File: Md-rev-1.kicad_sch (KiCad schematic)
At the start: 24 parts, among them CN1 JSTPH, J1 USB_C_Receptacle_USB2.0, J2 AudioJack4_SwitchTR1, U1 MCP73831-2-OT, U2 MAX9814

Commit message: Updated the schematic & PCB
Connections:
- net GND: no longer S1.2
- net VBAT: now also S1.2; no longer C2.1, S1.3, U1.3 (V_{BAT})
- net at S1.1: now also C2.1, U1.3 (V_{BAT})
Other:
- moved on the sheet: CN1, S1
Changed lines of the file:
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@@
   (junction (at 180.34 118.11) (diameter 0) (color 0 0 0 0)
   )
-  (junction (at 144.78 152.4) (diameter 0) (color 0 0 0 0)
+  (junction (at 158.75 121.92) (diameter 0) (color 0 0 0 0)
   )
   (junction (at 123.19 124.46) (diameter 0) (color 0 0 0 0)
@@
   (junction (at 34.29 148.59) (diameter 0) (color 0 0 0 0)
   )
-  (junction (at 147.32 124.46) (diameter 0) (color 0 0 0 0)
-  )
   (junction (at 92.71 120.65) (diameter 0) (color 0 0 0 0)
   )
@@
   )
   (no_connect (at 345.44 124.46))
-  (no_connect (at 142.24 130.81))
+  (no_connect (at 139.7 119.38))
   (no_connect (at 62.23 123.19))
   (no_connect (at 62.23 130.81))
@@
     (stroke (width 0) (type default))
   )
-  (wire (pts (xy 154.94 127) (xy 154.94 153.67))
+  (wire (pts (xy 154.94 124.46) (xy 154.94 153.67))
     (stroke (width 0) (type default))
   )
@@
     (stroke (width 0) (type default))
   )
-  (wire (pts (xy 154.94 127) (xy 162.56 127))
+  (wire (pts (xy 154.94 124.46) (xy 166.37 124.46))
     (stroke (width 0) (type default))
   )
@@
     (stroke (width 0) (type default))
   )
+  (wire (pts (xy 154.94 121.92) (xy 158.75 121.92))
+    (stroke (width 0) (type default))
+  )
   (wire (pts (xy 57.15 123.19) (xy 62.23 123.19))
     (stroke (width 0) (type default))
@@
     (stroke (width 0) (type default))
   )
-  (wire (pts (xy 144.78 146.05) (xy 144.78 152.4))
-    (stroke (width 0) (type default))
-  )
   (wire (pts (xy 105.41 124.46) (xy 123.19 124.46))
     (stroke (width 0) (type default))
@@
     (stroke (width 0) (type default))
   )
-  (wire (pts (xy 123.19 124.46) (xy 147.32 124.46))
-    (stroke (width 0) (type default))
-  )
   (wire (pts (xy 185.42 113.03) (xy 187.96 113.03))
     (stroke (width 0) (type default))
@@
     (stroke (width 0) (type default))
   )
-  (wire (pts (xy 144.78 152.4) (xy 144.78 153.67))
-    (stroke (width 0) (type default))
-  )
   (wire (pts (xy 285.75 120.65) (xy 297.18 120.65))
     (stroke (width 0) (type default))
@@
     (stroke (width 0) (type default))
   )
-  (wire (pts (xy 147.32 124.46) (xy 147.32 130.81))
-    (stroke (width 0) (type default))
-  )
   (wire (pts (xy 200.66 113.03) (xy 240.03 113.03))
     (stroke (width 0) (type default))
@@
     (stroke (width 0) (type default))
   )
-  (wire (pts (xy 147.32 124.46) (xy 162.56 124.46))
+  (wire (pts (xy 123.19 124.46) (xy 139.7 124.46))
     (stroke (width 0) (type default))
   )
@@
   )
   (wire (pts (xy 123.19 142.24) (xy 123.19 153.67))
+    (stroke (width 0) (type default))
+  )
+  (wire (pts (xy 158.75 121.92) (xy 166.37 121.92))
     (stroke (width 0) (type default))
   )
@@
     (effects (font (size 1.27 1.27)) (justify left bottom))
   )
-  (label "VBAT" (at 151.13 124.46 0) (fields_autoplaced)
+  (label "VBAT" (at 156.21 121.92 90) (fields_autoplaced)
     (effects (font (size 1.27 1.27)) (justify left bottom))
   )
@@
     )
   )
-  (symbol (lib_id "500SSP1S1M6QEA:500SSP1S1M6QEA") (at 144.78 138.43 90) (unit 1)
-    (in_bom yes) (on_board yes) (dnp no) (fields_autoplaced)
-    (property "Reference" "S1" (at 148.59 137.16 90)
-      (effects (font (size 1.27 1.27)) (justify right))
-    )
-    (property "Value" "500SSP1S1M6QEA" (at 148.59 139.7 90)
-      (effects (font (size 1.27 1.27)) (justify right))
-    )
-    (property "Footprint" "500SSP1S1M6QEA:SW_500SSP1S1M6QEA" (at 144.78 138.43 0)
-      (effects (font (size 1.27 1.27)) (justify bottom) hide)
-    )
-    (property "Datasheet" "" (at 144.78 138.43 0)
-      (effects (font (size 1.27 1.27)) hide)
-    )
-    (property "MF" "E-Switch" (at 144.78 138.43 0)
-      (effects (font (size 1.27 1.27)) (justify bottom) hide)
-    )
-    (property "Description" "\nSlide Switch, 500A Series, DPDT, ON-ON, 5A, 120VAC/28VDC, Silver, R/A PC Pin | E-Switch 500SSP1S1M6QEA\n" (at 144.78 138.43 0)
-      (effects (font (size 1.27 1.27)) (justify bottom) hide)
-    )
-    (property "Package" "None" (at 144.78 138.43 0)
-      (effects (font (size 1.27 1.27)) (justify bottom) hide)
-    )
-    (property "Price" "None" (at 144.78 138.43 0)
-      (effects (font (size 1.27 1.27)) (justify bottom) hide)
-    )
-    (property "Check_prices" "https://www.snapeda.com/parts/500SSP1S1M6QEA/E-Switch/view-part/?ref=eda" (at 144.78 138.43 0)
-      (effects (font (size 1.27 1.27)) (justify bottom) hide)
-    )
-    (property "SnapEDA_Link" "https://www.snapeda.com/parts/500SSP1S1M6QEA/E-Switch/view-part/?ref=snap" (at 144.78 138.43 0)
-      (effects (font (size 1.27 1.27)) (justify bottom) hide)
-    )
-    (property "MP" "500SSP1S1M6QEA" (at 144.78 138.43 0)
-      (effects (font (size 1.27 1.27)) (justify bottom) hide)
-    )
-    (property "Availability" "In Stock" (at 144.78 138.43 0)
-      (effects (font (size 1.27 1.27)) (justify bottom) hide)
-    )
-    (property "Purchase-URL" "https://www.snapeda.com/api/url_track_click_mouser/?unipart_id=488032&manufacturer=E-Switch&part_name=500SSP1S1M6QEA&search_term=spdt" (at 144.78 138.43 0)
+  (symbol (lib_id "500SSP1S1M6QEA:500SSP1S1M6QEA") (at 147.32 121.92 180) (unit 1)
+    (in_bom yes) (on_board yes) (dnp no)
+    (property "Reference" "S1" (at 144.78 111.76 90)
+      (effects (font (size 1.27 1.27)))
+    )
+    (property "Value" "500SSP1S1M6QEA" (at 147.32 113.03 90)
+      (effects (font (size 1.27 1.27)))
+    )
+    (property "Footprint" "500SSP1S1M6QEA:SW_500SSP1S1M6QEA" (at 147.32 121.92 0)
+      (effects (font (size 1.27 1.27)) (justify bottom) hide)
+    )
+    (property "Datasheet" "" (at 147.32 121.92 0)
+      (effects (font (size 1.27 1.27)) hide)
+    )
+    (property "MF" "E-Switch" (at 147.32 121.92 0)
+      (effects (font (size 1.27 1.27)) (justify bottom) hide)
+    )
+    (property "Description" "\nSlide Switch, 500A Series, DPDT, ON-ON, 5A, 120VAC/28VDC, Silver, R/A PC Pin | E-Switch 500SSP1S1M6QEA\n" (at 147.32 121.92 0)
+      (effects (font (size 1.27 1.27)) (justify bottom) hide)
+    )
+    (property "Package" "None" (at 147.32 121.92 0)
+      (effects (font (size 1.27 1.27)) (justify bottom) hide)
+    )
+    (property "Price" "None" (at 147.32 121.92 0)
+      (effects (font (size 1.27 1.27)) (justify bottom) hide)
+    )
+    (property "Check_prices" "https://www.snapeda.com/parts/500SSP1S1M6QEA/E-Switch/view-part/?ref=eda" (at 147.32 121.92 0)
+      (effects (font (size 1.27 1.27)) (justify bottom) hide)
+    )
+    (property "SnapEDA_Link" "https://www.snapeda.com/parts/500SSP1S1M6QEA/E-Switch/view-part/?ref=snap" (at 147.32 121.92 0)
+      (effects (font (size 1.27 1.27)) (justify bottom) hide)
+    )
+    (property "MP" "500SSP1S1M6QEA" (at 147.32 121.92 0)
+      (effects (font (size 1.27 1.27)) (justify bottom) hide)
+    )
+    (property "Availability" "In Stock" (at 147.32 121.92 0)
+      (effects (font (size 1.27 1.27)) (justify bottom) hide)
+    )
+    (property "Purchase-URL" "https://www.snapeda.com/api/url_track_click_mouser/?unipart_id=488032&manufacturer=E-Switch&part_name=500SSP1S1M6QEA&search_term=spdt" (at 147.32 121.92 0)
       (effects (font (size 1.27 1.27)) (justify bottom) hide)
     )
@@
     )
   )
-  (symbol (lib_id "power:PWR_FLAG") (at 144.78 152.4 270) (unit 1)
+  (symbol (lib_id "power:PWR_FLAG") (at 158.75 121.92 0) (unit 1)
     (in_bom yes) (on_board yes) (dnp no)
-    (property "Reference" "#FLG02" (at 146.685 152.4 0)
-      (effects (font (size 1.27 1.27)) hide)
-    )
-    (property "Value" "PWR_FLAG" (at 144.78 149.86 90)
+    (property "Reference" "#FLG02" (at 158.75 120.015 0)
+      (effects (font (size 1.27 1.27)) hide)
+    )
+    (property "Value" "PWR_FLAG" (at 158.75 119.38 90)
       (effects (font (size 1.27 1.27)) (justify left))
     )
-    (property "Footprint" "" (at 144.78 152.4 0)
-      (effects (font (size 1.27 1.27)) hide)
-    )
-    (property "Datasheet" "~" (at 144.78 152.4 0)
+    (property "Footprint" "" (at 158.75 121.92 0)
+      (effects (font (size 1.27 1.27)) hide)
+    )
+    (property "Datasheet" "~" (at 158.75 121.92 0)
       (effects (font (size 1.27 1.27)) hide)
     )
@@
     )
   )
-  (symbol (lib_id "power:GND") (at 144.78 153.67 0) (unit 1)
-    (in_bom yes) (on_board yes) (dnp no) (fields_autoplaced)
-    (property "Reference" "#PWR08" (at 144.78 160.02 0)
-      (effects (font (size 1.27 1.27)) hide)
-    )
-    (property "Value" "GND" (at 144.78 158.75 0)
-      (effects (font (size 1.27 1.27)))
-    )
-    (property "Footprint" "" (at 144.78 153.67 0)
-      (effects (font (size 1.27 1.27)) hide)
-    )
-    (property "Datasheet" "" (at 144.78 153.67 0)
-      (effects (font (size 1.27 1.27)) hide)
-    )
-    (pin "1")
-    (instances
-      (project "Md-rev-1"
-        (path "/34e1f0a2-75b5-46dc-b967-b4433c15cc45"
-          (reference "#PWR08") (unit 1)
-        )
-      )
-    )
-  )
   (symbol (lib_id "Device:C") (at 123.19 138.43 0) (unit 1)
     (in_bom yes) (on_board yes) (dnp no)
@@
     )
   )
-  (symbol (lib_id "Adafruit USB C microlipo charger-eagle-import:JST_2PIN") (at 160.02 124.46 180) (unit 1)
+  (symbol (lib_id "Adafruit USB C microlipo charger-eagle-import:JST_2PIN") (at 163.83 121.92 180) (unit 1)
     (in_bom yes) (on_board yes) (dnp no)
-    (property "Reference" "CN1" (at 166.37 130.175 0)
+    (property "Reference" "CN1" (at 170.18 127.635 0)
       (effects (font (size 1.778 1.5113)) (justify left bottom))
     )
-    (property "Value" "JSTPH" (at 166.37 119.38 0)
+    (property "Value" "JSTPH" (at 170.18 116.84 0)
       (effects (font (size 1.778 1.5113)) (justify left bottom))
     )
-    (property "Footprint" "Connector_JST:JST_PH_S2B-PH-K_1x02_P2.00mm_Horizontal" (at 160.02 124.46 0)
-      (effects (font (size 1.27 1.27)) hide)
-    )
-    (property "Datasheet" "" (at 160.02 124.46 0)
-      (effects (font (size 1.27 1.27)) hide)
-    )
+    (property "Footprint" "Connector_JST:JST_PH_S2B-PH-K_1x02_P2.00mm_Horizontal" (at 163.83 121.92 0)
+      (effects (font (size 1.27 1.27)) hide)
+    )
+    (property "Datasheet" "" (at 163.83 121.92 0)
+      (effects (font (size 1.27 1.27)) hide)
+    )

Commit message: Updated the footprint files
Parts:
- MK1: footprint Buzzer_Beeper:MagneticBuzzer_Kingstate_KCG0601 -> Buzzer_Beeper:MagneticBuzzer_Kobitone_254-EMB73-RO
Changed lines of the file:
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@@
       (effects (font (size 1.27 1.27)))
     )
-    (property "Footprint" "Buzzer_Beeper:MagneticBuzzer_Kingstate_KCG0601" (at 207.01 128.27 90)
+    (property "Footprint" "Buzzer_Beeper:MagneticBuzzer_Kobitone_254-EMB73-RO" (at 207.01 128.27 90)
       (effects (font (size 1.27 1.27)) hide)
     )

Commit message: New meditation device layout
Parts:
- removed S1: 500SSP1S1M6QEA, 500SSP1S1M6QEA:SW_500SSP1S1M6QEA, symbol 500SSP1S1M6QEA:500SSP1S1M6QEA
- added C7: 10uF, Capacitor_SMD:C_0805_2012Metric, symbol Device:C
- added S1: 500ASSP1SM6QE, 500ASSP1SM6QE:SW_500ASSP1SM6QE, symbol 500ASSP1SM6QE:500ASSP1SM6QE
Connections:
- net VBAT is gone; now on net GAIN: CN1.2, U2.2 (~{SHDN}), U2.5 (VDD)
- net GAIN: now also S1.2
- net OUTPUT: now also C7.2; no longer U2.6 (MICOUT)
- net at C2.1, U1.3 (V_{BAT}): now also S1.1
- new net: C7.1, U2.6 (MICOUT)
- no-connect marks 13 -> 12

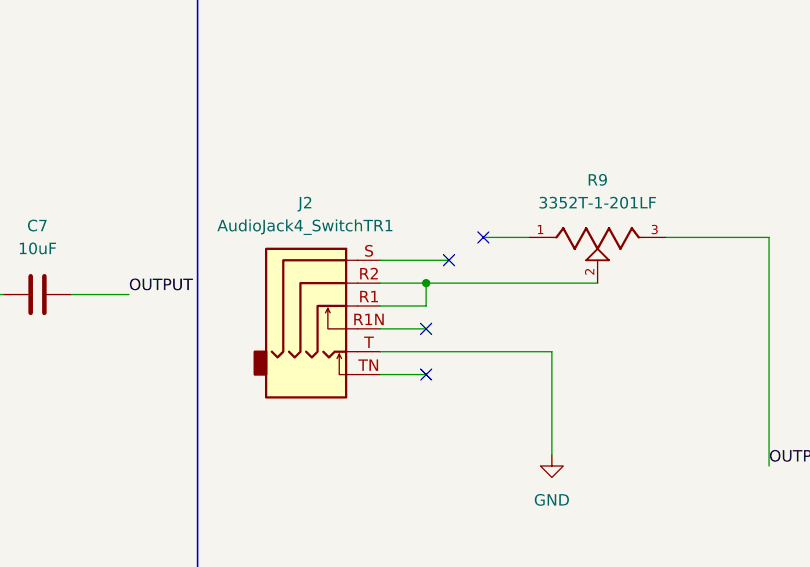
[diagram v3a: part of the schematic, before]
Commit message: Updated the footprint to reflect the newTRRS headphone jack
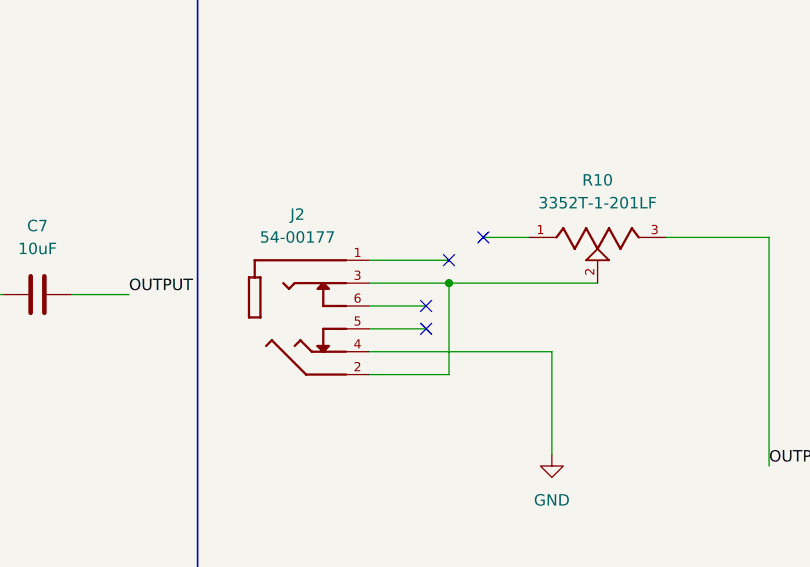
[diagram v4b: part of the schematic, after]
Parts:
- removed J2: AudioJack4_SwitchTR1, Connector_Audio:Jack_3.5mm_PJ31060-I_Horizontal, symbol Connector_Audio:AudioJack4_SwitchTR1
- added J2: 54-00177, 54-00177:TENSILITY_54-00177, symbol 54-00177:54-00177
- renumbered R9 to R10
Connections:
- net GND: now also J2.4
- net at R10.2: now also J2.2, J2.3
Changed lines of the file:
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@@
   (junction (at 158.75 121.92) (diameter 0) (color 0 0 0 0)
   )
+  (junction (at 347.98 119.38) (diameter 0) (color 0 0 0 0)
+  )
   (junction (at 123.19 124.46) (diameter 0) (color 0 0 0 0)
   )
@@
   (junction (at 200.66 113.03) (diameter 0) (color 0 0 0 0)
   )
-  (junction (at 345.44 119.38) (diameter 0) (color 0 0 0 0)
-  )
   (junction (at 215.9 118.11) (diameter 0) (color 0 0 0 0)
   )
   (junction (at 215.9 128.27) (diameter 0) (color 0 0 0 0)
   )
-  (no_connect (at 345.44 124.46))
   (no_connect (at 139.7 119.38))
   (no_connect (at 62.23 123.19))
   (no_connect (at 62.23 130.81))
+  (no_connect (at 345.44 121.92))
   (no_connect (at 347.98 116.84))
   (no_connect (at 234.95 110.49))
+  (no_connect (at 345.44 124.46))
   (no_connect (at 351.79 114.3))
   (no_connect (at 62.23 138.43))
-  (no_connect (at 345.44 129.54))
   (no_connect (at 62.23 140.97))
   (no_connect (at 62.23 125.73))
@@
     (stroke (width 0) (type default))
   )
-  (wire (pts (xy 345.44 119.38) (xy 364.49 119.38))
+  (wire (pts (xy 339.09 119.38) (xy 347.98 119.38))
     (stroke (width 0) (type default))
   )
@@
     (stroke (width 0) (type default))
   )
+  (wire (pts (xy 339.09 127) (xy 359.41 127))
+    (stroke (width 0) (type default))
+  )
   (wire (pts (xy 57.15 115.57) (xy 74.93 115.57))
     (stroke (width 0) (type default))
@@
     (stroke (width 0) (type default))
   )
-  (wire (pts (xy 345.44 119.38) (xy 345.44 121.92))
-    (stroke (width 0) (type default))
-  )
   (wire (pts (xy 208.28 118.11) (xy 215.9 118.11))
     (stroke (width 0) (type default))
@@
     (stroke (width 0) (type default))
   )
+  (wire (pts (xy 339.09 129.54) (xy 347.98 129.54))
+    (stroke (width 0) (type default))
+  )
   (wire (pts (xy 57.15 123.19) (xy 62.23 123.19))
     (stroke (width 0) (type default))
@@
     (stroke (width 0) (type default))
   )
+  (wire (pts (xy 339.09 124.46) (xy 345.44 124.46))
+    (stroke (width 0) (type default))
+  )
   (wire (pts (xy 180.34 148.59) (xy 180.34 118.11))
     (stroke (width 0) (type default))
@@
     (stroke (width 0) (type default))
   )
+  (wire (pts (xy 347.98 129.54) (xy 347.98 119.38))
+    (stroke (width 0) (type default))
+  )
   (wire (pts (xy 209.55 128.27) (xy 215.9 128.27))
     (stroke (width 0) (type default))
@@
     (stroke (width 0) (type default))
   )
-  (wire (pts (xy 340.36 116.84) (xy 347.98 116.84))
+  (wire (pts (xy 339.09 116.84) (xy 347.98 116.84))
+    (stroke (width 0) (type default))
+  )
+  (wire (pts (xy 347.98 119.38) (xy 364.49 119.38))
     (stroke (width 0) (type default))
   )
@@
     (stroke (width 0) (type default))
   )
-  (wire (pts (xy 340.36 127) (xy 359.41 127))
-    (stroke (width 0) (type default))
-  )
   (wire (pts (xy 123.19 124.46) (xy 123.19 134.62))
     (stroke (width 0) (type default))
@@
     (stroke (width 0) (type default))
   )
-  (wire (pts (xy 340.36 124.46) (xy 345.44 124.46))
-    (stroke (width 0) (type default))
-  )
   (wire (pts (xy 57.15 110.49) (xy 69.85 110.49))
     (stroke (width 0) (type default))
@@
     (stroke (width 0) (type default))
   )
-  (wire (pts (xy 340.36 119.38) (xy 345.44 119.38))
-    (stroke (width 0) (type default))
-  )
-  (wire (pts (xy 340.36 121.92) (xy 345.44 121.92))
-    (stroke (width 0) (type default))
-  )
-  (wire (pts (xy 340.36 129.54) (xy 345.44 129.54))
+  (wire (pts (xy 339.09 121.92) (xy 345.44 121.92))
     (stroke (width 0) (type default))
   )
@@
         (path "/34e1f0a2-75b5-46dc-b967-b4433c15cc45"
           (reference "U2") (unit 1)
+        )
+      )
+    )
+  )
+  (symbol (lib_id "54-00177:54-00177") (at 331.47 121.92 0) (unit 1)
+    (in_bom yes) (on_board yes) (dnp no) (fields_autoplaced)
+    (property "Reference" "J2" (at 331.1525 111.76 0)
+      (effects (font (size 1.27 1.27)))
+    )
+    (property "Value" "54-00177" (at 331.1525 114.3 0)
+      (effects (font (size 1.27 1.27)))
+    )
+    (property "Footprint" "54-00177:TENSILITY_54-00177" (at 331.47 121.92 0)
+      (effects (font (size 1.27 1.27)) (justify bottom) hide)
+    )
+    (property "Datasheet" "" (at 331.47 121.92 0)
+      (effects (font (size 1.27 1.27)) hide)
+    )
+    (property "PARTREV" "A" (at 331.47 121.92 0)
+      (effects (font (size 1.27 1.27)) (justify bottom) hide)
+    )
+    (property "STANDARD" "Manufacturer Recommendations" (at 331.47 121.92 0)
+      (effects (font (size 1.27 1.27)) (justify bottom) hide)
+    )
+    (property "SNAPEDA_PN" "54-00177" (at 331.47 121.92 0)
+      (effects (font (size 1.27 1.27)) (justify bottom) hide)
+    )
+    (property "MAXIMUM_PACKAGE_HEIGHT" "4.5mm" (at 331.47 121.92 0)
+      (effects (font (size 1.27 1.27)) (justify bottom) hide)
+    )
+    (property "MANUFACTURER" "TENSILITY" (at 331.47 121.92 0)
+      (effects (font (size 1.27 1.27)) (justify bottom) hide)
+    )
+    (pin "1")
+    (pin "2")
+    (pin "3")
+    (pin "4")
+    (pin "5")
+    (pin "6")
+    (instances
+      (project "Md-rev-1"
+        (path "/34e1f0a2-75b5-46dc-b967-b4433c15cc45"
+          (reference "J2") (unit 1)
         )
       )
@@
     )
   )
-  (symbol (lib_id "Connector_Audio:AudioJack4_SwitchTR1") (at 335.28 121.92 0) (unit 1)
-    (in_bom yes) (on_board yes) (dnp no) (fields_autoplaced)
-    (property "Reference" "J2" (at 332.0415 110.49 0)
-      (effects (font (size 1.27 1.27)))
-    )
-    (property "Value" "AudioJack4_SwitchTR1" (at 332.0415 113.03 0)
-      (effects (font (size 1.27 1.27)))
-    )
-    (property "Footprint" "Connector_Audio:Jack_3.5mm_PJ31060-I_Horizontal" (at 334.01 121.92 0)
-      (effects (font (size 1.27 1.27)) hide)
-    )
-    (property "Datasheet" "~" (at 334.01 121.92 0)
-      (effects (font (size 1.27 1.27)) hide)
-    )
-    (pin "R1")
-    (pin "R1N")
-    (pin "R2")
-    (pin "S")
-    (pin "T")
-    (pin "TN")
-    (instances
-      (project "Md-rev-1"
-        (path "/34e1f0a2-75b5-46dc-b967-b4433c15cc45"
-          (reference "J2") (unit 1)
-        )
-      )
-    )
-  )
   (symbol (lib_id "Device:Microphone_Condenser") (at 204.47 128.27 270) (unit 1)
     (in_bom yes) (on_board yes) (dnp no) (fields_autoplaced)
@@
   (symbol (lib_id "3352T-1-201LF:3352T-1-201LF") (at 364.49 114.3 0) (unit 1)
     (in_bom yes) (on_board yes) (dnp no) (fields_autoplaced)
-    (property "Reference" "R9" (at 364.49 107.95 0)
+    (property "Reference" "R10" (at 364.49 107.95 0)
       (effects (font (size 1.27 1.27)))
     )
@@
       (project "Md-rev-1"
         (path "/34e1f0a2-75b5-46dc-b967-b4433c15cc45"
-          (reference "R9") (unit 1)
+          (reference "R10") (unit 1)
         )
       )
@@
   (symbol (lib_id "power:GND") (at 359.41 138.43 0) (unit 1)
     (in_bom yes) (on_board yes) (dnp no) (fields_autoplaced)
-    (property "Reference" "#PWR014" (at 359.41 144.78 0)
+    (property "Reference" "#PWR015" (at 359.41 144.78 0)
       (effects (font (size 1.27 1.27)) hide)
     )
@@
       (project "Md-rev-1"
         (path "/34e1f0a2-75b5-46dc-b967-b4433c15cc45"
-          (reference "#PWR014") (unit 1)
-        )
-      )
+          (reference "#PWR015") (unit 1)
+        )
+      )
